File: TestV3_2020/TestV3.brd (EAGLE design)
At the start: 100 x 100 mm, 116 parts, among them J11 CONN_03, J4 XT30UPB-F, J5 CONN_03, J6 XT30UPB-F, Q3 600mA/40V, Q4 600mA/40V, U2 MP2451, U4 LIGHT_SENSORALS

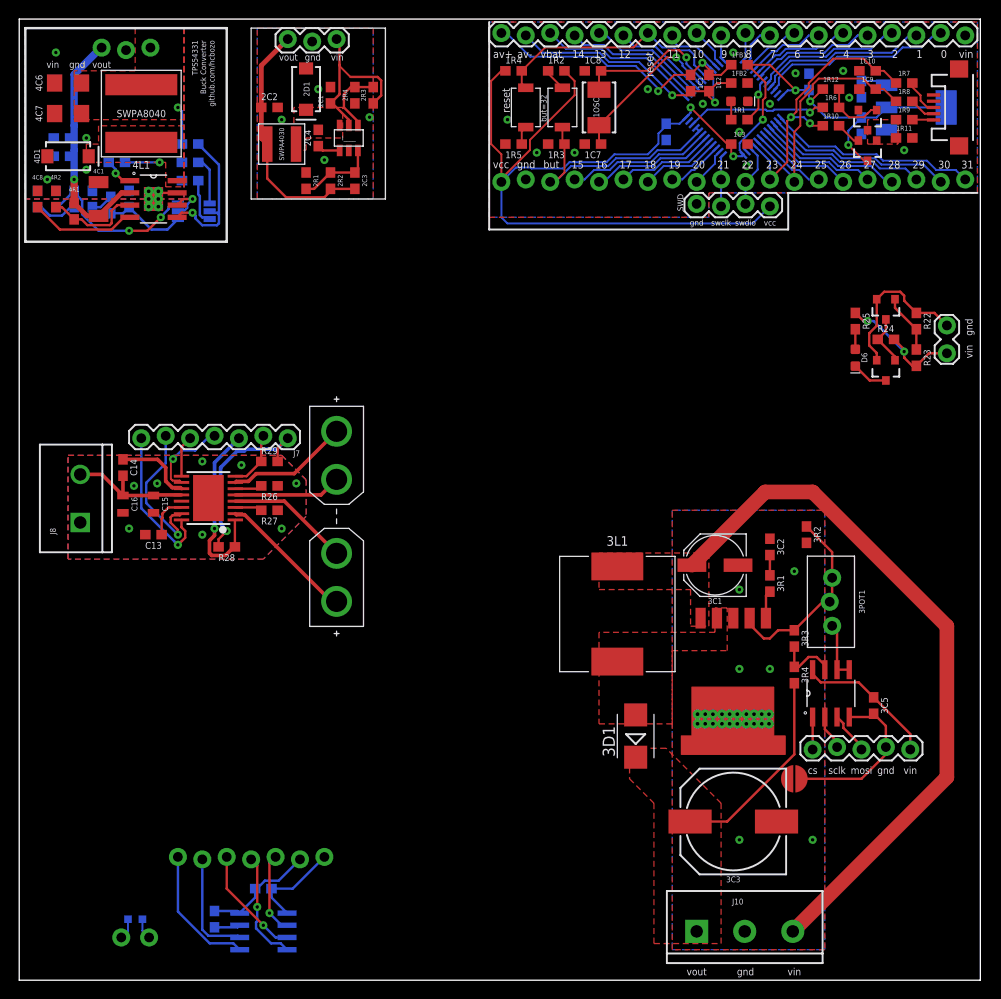
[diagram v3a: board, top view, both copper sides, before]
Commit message: added more light sensors and lights to test and optimise positioning, added xt60 for test fitting
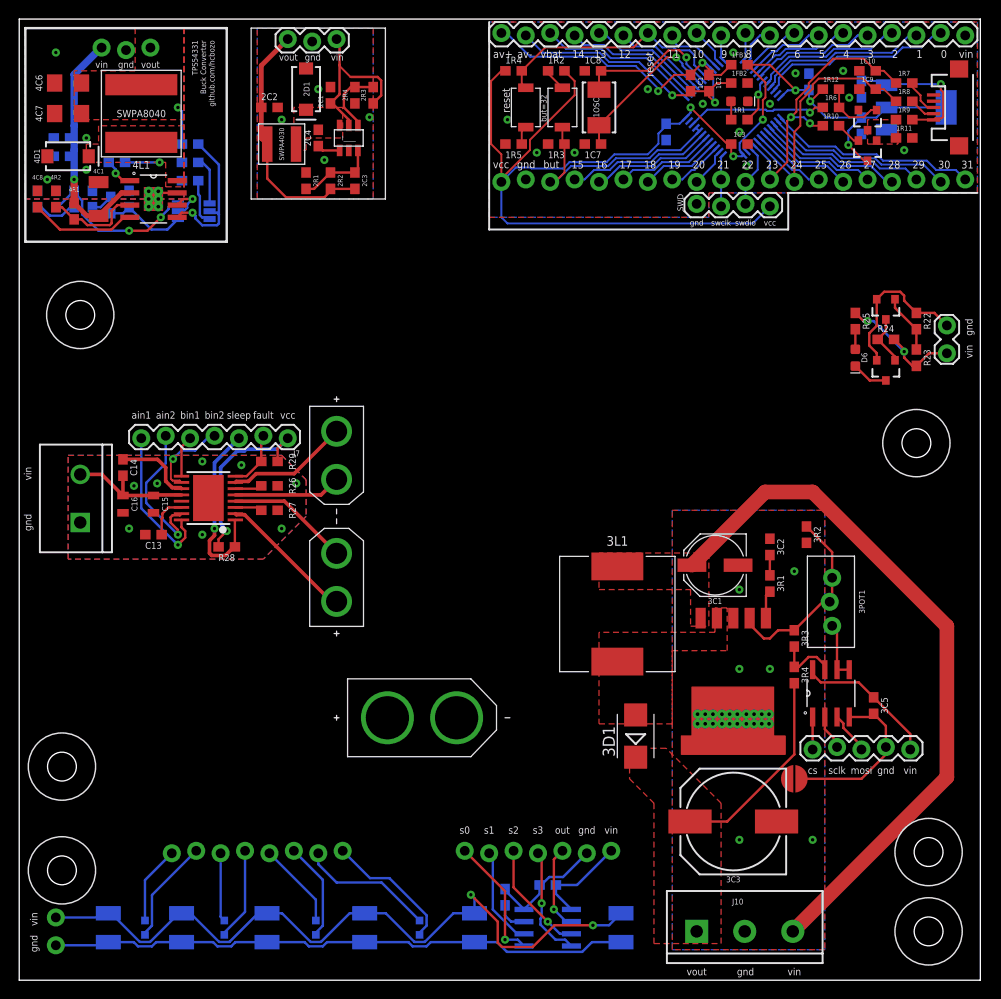
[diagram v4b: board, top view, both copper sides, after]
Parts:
- added D1, D2, D3, D4, D5, D7: 3528LED, JH:3528
- added J12: (no value), SparkFun-Connectors:1X02_LOCK
- added J13: XT60PB-F, JH:XT60PB-F
- added U6, U7, U8: LIGHT_SENSORALS, SparkFun-Sensors:ALS-PT19
- J3: device SparkFun-Connectors:1X02_LOCK -> SparkFun-Connectors:1X08_LOCK
- moved R30 30.3 mm to (50.5, 8.64)
- moved J1 29.9 mm to (61.6, 13.3)
- moved C20 29.6 mm to (55.0, 9.91)
- moved CS1 29.6 mm to (55.0, 5.46)
- moved J3 9.25 mm to (15.9, 13.3), turned to 180 degrees
- moved U4 1.35 mm to (13.1, 5.46), turned to 90 degrees
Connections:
- new net N$19: J3.4, U6.C
- new net N$56: J3.3, U6.E
- new net N$61: J3.8, U7.C
- new net N$62: J3.7, U7.E
- new net N$63: J3.5, U8.E
- new net N$64: J3.6, U8.C
- new net N$7: D1.A, D2.A, D3.A, D4.A, D5.A, D7.A, J12.2
- net N$13: now also D1.C, D2.C, D3.C, D4.C, D5.C, D7.C, J12.1; no longer 1C5.1, 1U2.3
- net V_USB: now also 1C5.1, 1U2.3
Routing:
- net N$7: track 0.00 -> 76.3 mm, vias 0 -> 2
- net N$13: track 2.80 -> 61.2 mm
- net N$62: track 0.00 -> 14.1 mm
- net N$61: track 0.00 -> 13.9 mm
- net V_USB: track 2.23 -> 15.4 mm, vias 0 -> 1
- net N$64: track 0.00 -> 10.3 mm
- net N$19: track 0.00 -> 9.65 mm
- net N$63: track 0.00 -> 9.00 mm
- net N$14: track 2.19 -> 11.0 mm
- net N$56: track 0.00 -> 7.15 mm
- net N$17: track 2.19 -> 8.15 mm
- net N$46: track 11.5 -> 10.3 mm
- net GND-CS: track 11.8 -> 12.4 mm
- net N$50: track 2.71 -> 3.30 mm
- net N$45: track 13.8 -> 13.2 mm, vias 0 -> 1
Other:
- board text added: "ain1"
- board text added: "ain2"
- board text added: "bin1"
- board text added: "bin2"
- board text added: "fault"
- board text added: "out"
- board text added: "s0"
- board text added: "s1"
- board text added: "s2"
- board text added: "s3"
- board text added: "sleep"
- board text removed: "light sensor test"

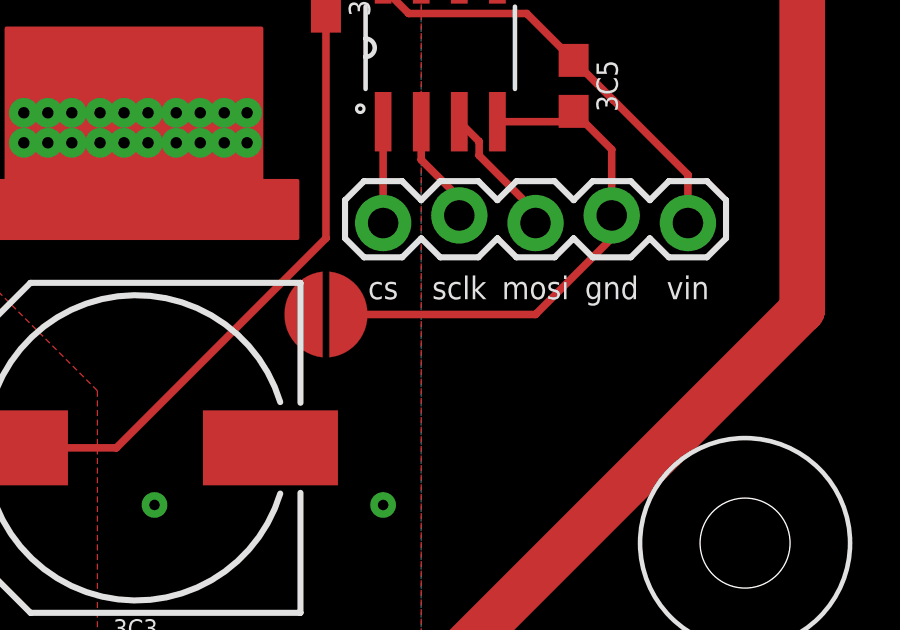
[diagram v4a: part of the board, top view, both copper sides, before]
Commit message: minor changes, mostly fixed the values of some components
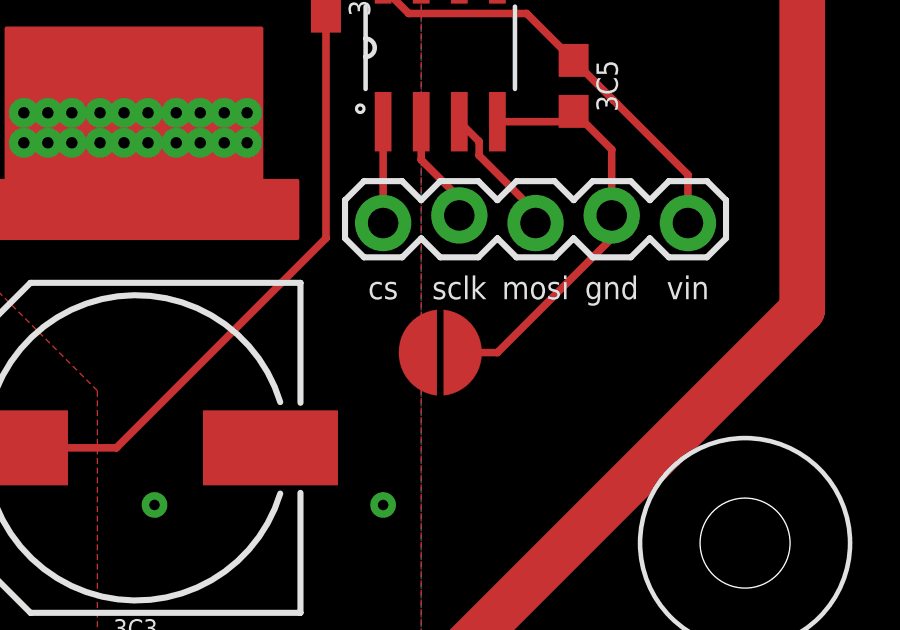
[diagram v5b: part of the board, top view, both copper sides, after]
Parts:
- 3R4: value 45k -> 47k
- 4C11: value 4.7nF -> 4700pF
- R28: value 20k-75k -> 47k
- moved JP1 4.02 mm to (84.5, 19.7)
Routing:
- net GND-POT: track 16.7 -> 13.5 mm
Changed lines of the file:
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@@
 <attribute name="VALUE" x="1.905" y="79.248" size="0.4572" layer="28" font="vector" ratio="16" rot="MR0" align="top-center"/>
 </element>
-<element name="4C11" library="JH" library_urn="urn:adsk.eagle:library:6027132" package="C0603" package3d_urn="urn:adsk.eagle:package:15441226/3" value="4.7nF" x="5.715" y="81.28" smashed="yes" rot="MR270">
+<element name="4C11" library="JH" library_urn="urn:adsk.eagle:library:6027132" package="C0603" package3d_urn="urn:adsk.eagle:package:15441226/3" value="4700pF" x="5.715" y="81.28" smashed="yes" rot="MR270">
 <attribute name="NAME" x="5.715" y="83.312" size="0.4572" layer="26" font="vector" ratio="16" rot="MR0" align="bottom-center"/>
 <attribute name="VALUE" x="5.715" y="79.248" size="0.4572" layer="28" font="vector" ratio="16" rot="MR0" align="top-center"/>
@@
 <attribute name="VALUE" x="81.534" y="39.37" size="0.6096" layer="27" font="vector" ratio="18" rot="R270" align="top-center"/>
 </element>
-<element name="3R4" library="JH" library_urn="urn:adsk.eagle:library:6027132" package="R0603" package3d_urn="urn:adsk.eagle:package:15441228/3" value="45k" x="80.645" y="31.75" smashed="yes" rot="R270">
+<element name="3R4" library="JH" library_urn="urn:adsk.eagle:library:6027132" package="R0603" package3d_urn="urn:adsk.eagle:package:15441228/3" value="47k" x="80.645" y="31.75" smashed="yes" rot="R270">
 <attribute name="NAME" x="81.407" y="31.75" size="0.7112" layer="25" font="vector" ratio="18" rot="R270" align="bottom-center"/>
 <attribute name="VALUE" x="79.883" y="31.75" size="0.7112" layer="27" font="vector" ratio="18" rot="R270" align="top-center"/>
@@
 <attribute name="VOLTAGE" value="16V" x="12.065" y="55.88" size="1.778" layer="27" rot="R270" display="off"/>
 </element>
-<element name="R28" library="JH" library_urn="urn:adsk.eagle:library:6027132" package="R0603" package3d_urn="urn:adsk.eagle:package:15441228/3" value="20k-75k" x="21.59" y="45.085" smashed="yes" rot="R180">
+<element name="R28" library="JH" library_urn="urn:adsk.eagle:library:6027132" package="R0603" package3d_urn="urn:adsk.eagle:package:15441228/3" value="47k" x="21.59" y="45.085" smashed="yes" rot="R180">
 <attribute name="NAME" x="21.59" y="44.323" size="0.7112" layer="25" font="vector" ratio="18" rot="R180" align="bottom-center"/>
 <attribute name="VALUE" x="21.59" y="45.847" size="0.7112" layer="27" font="vector" ratio="18" rot="R180" align="top-center"/>
@@
 <attribute name="VALUE" x="36.83" y="94.107" size="0.508" layer="27" font="vector" ratio="18" rot="R180" align="top-center"/>
 </element>
-<element name="JP1" library="SparkFun-Jumpers" library_urn="urn:adsk.eagle:library:528" package="SMT-JUMPER_2_NO_NO-SILK_ROUND" package3d_urn="urn:adsk.eagle:package:39278/1" value="JUMPER-SMT_2_NO_NO-SILK_ROUND" x="80.645" y="20.955" smashed="yes"/>
+<element name="JP1" library="SparkFun-Jumpers" library_urn="urn:adsk.eagle:library:528" package="SMT-JUMPER_2_NO_NO-SILK_ROUND" package3d_urn="urn:adsk.eagle:package:39278/1" value="JUMPER-SMT_2_NO_NO-SILK_ROUND" x="84.455" y="19.685" smashed="yes"/>
 <element name="J12" library="SparkFun-Connectors" library_urn="urn:adsk.eagle:library:513" package="1X02_LOCK" package3d_urn="urn:adsk.eagle:package:38045/1" value="" x="3.81" y="3.81" smashed="yes" rot="MR90">
 <attribute name="NAME" x="5.207" y="2.54" size="0.6096" layer="26" font="vector" ratio="20" rot="MR90"/>
@@
 <contactref element="U3" pad="4"/>
 <contactref element="JP1" pad="2"/>
-<wire x1="81.915" y1="20.955" x2="87.63" y2="20.955" width="0.254" layer="1"/>
+<wire x1="85.725" y1="19.685" x2="86.36" y2="19.685" width="0.254" layer="1"/>
 <wire x1="88.9" y1="27.725" x2="88.5562" y2="27.3812" width="0.254" layer="1"/>
 <wire x1="88.5562" y1="27.3812" x2="86.36" y2="27.3812" width="0.254" layer="1"/>
 <contactref element="J2" pad="2"/>
-<wire x1="87.63" y1="20.955" x2="90.17" y2="23.495" width="0.254" layer="1"/>
+<wire x1="86.36" y1="19.685" x2="90.17" y2="23.495" width="0.254" layer="1"/>
 <wire x1="90.17" y1="23.495" x2="90.17" y2="24.257" width="0.254" layer="1"/>
 <wire x1="88.9" y1="27.725" x2="90.17" y2="26.455" width="0.254" layer="1"/>
